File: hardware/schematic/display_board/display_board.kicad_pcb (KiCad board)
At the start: 2 copper layers, 52.5 x 49 mm, 7 parts, among them J1 Conn_01x04_Pin, SW1 SW_Push, SW2 SW_Push

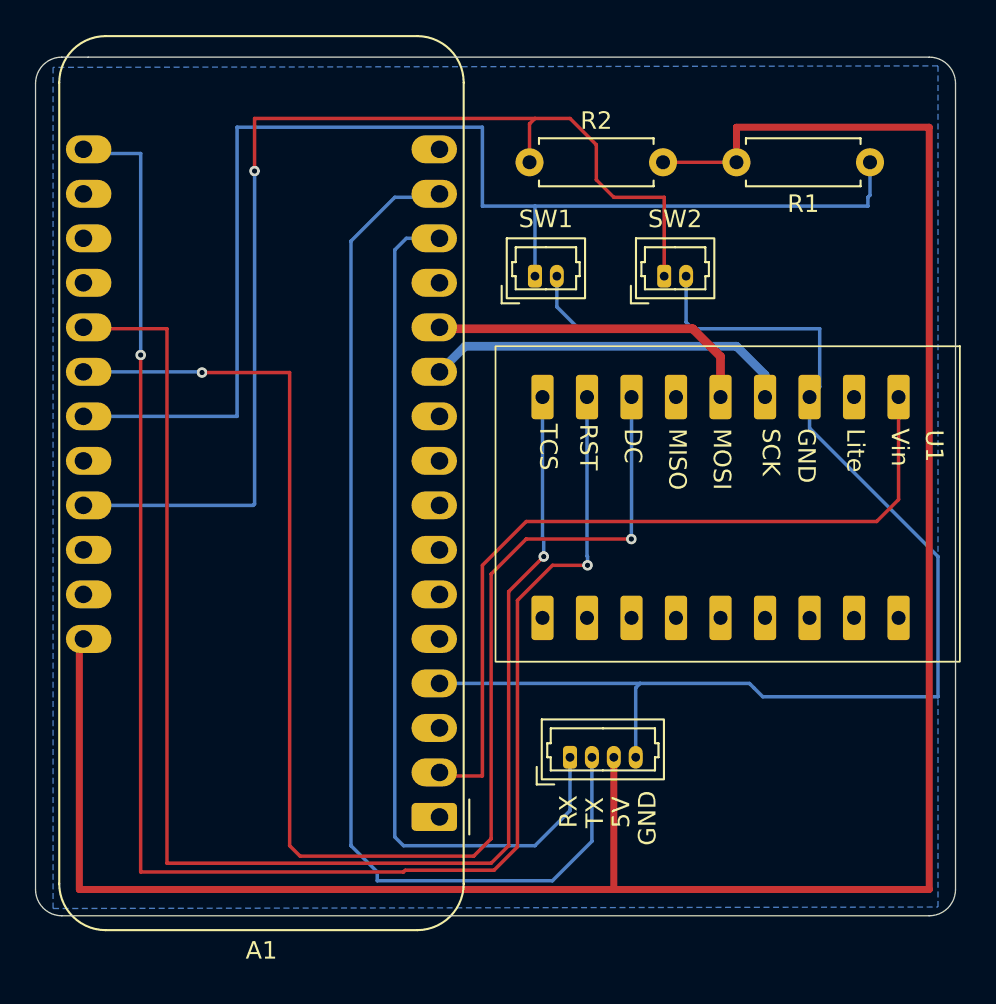
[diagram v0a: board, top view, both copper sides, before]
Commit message: First commit of PCB files for NAV and DISPLAY boards
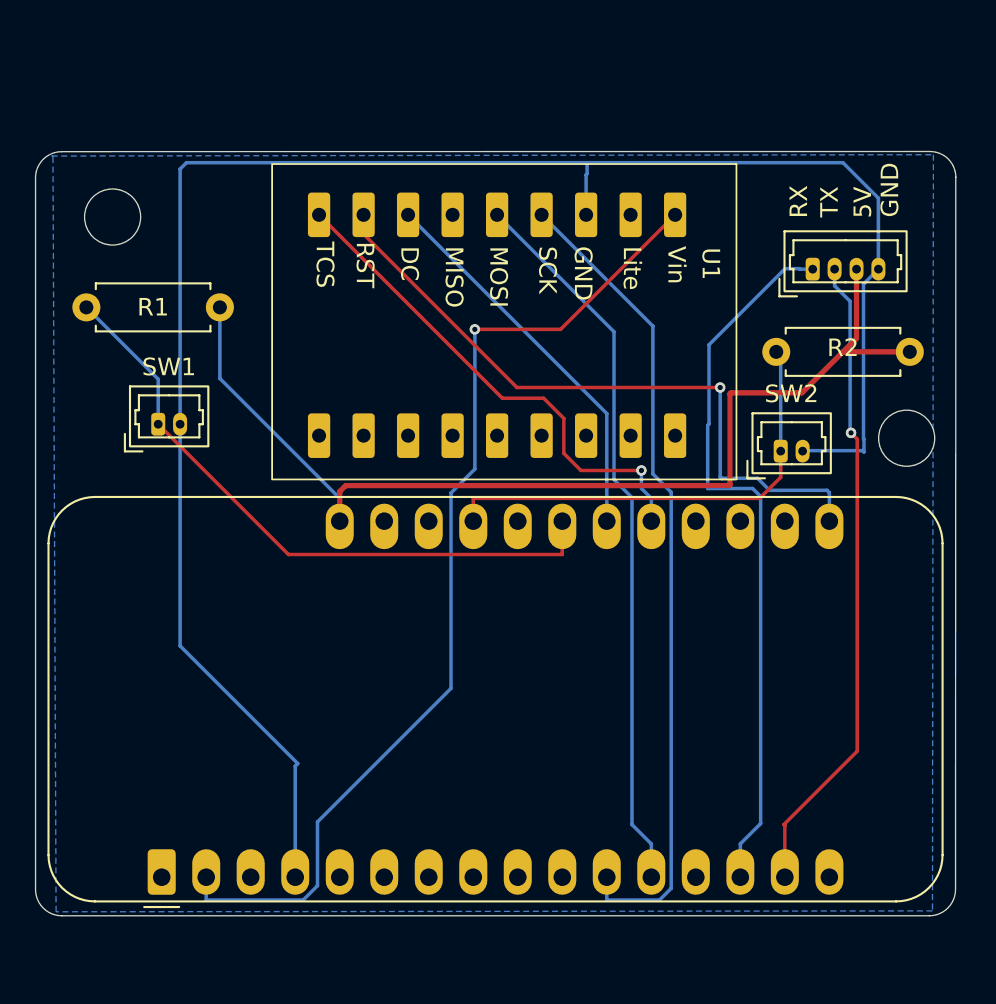
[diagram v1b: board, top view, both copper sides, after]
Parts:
- added REF**: MountingHole_3.2mm_M3_DIN965, MountingHole:MountingHole_3.2mm_M3_DIN965, F.Cu at (135.7, 88.7)
- added REF**: MountingHole_3.2mm_M3_DIN965, MountingHole:MountingHole_3.2mm_M3_DIN965, F.Cu at (90.4, 76.1)
- moved R1 45.5 mm to (88.9, 81.3), turned to 0 degrees
- moved J1 31.1 mm to (130.3, 79.1)
- moved SW1 23.1 mm to (93.0, 88.0)
- moved R2 17.8 mm to (128.3, 83.8)
- moved U1 16.5 mm to (122.5, 76.0)
- moved A1 16.2 mm to (93.2, 113.8), turned to 90 degrees
- moved SW2 12.0 mm to (128.5, 89.5)
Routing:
- net +5V: track 130.9 -> 60.9 mm
- net Net-(A1-A9/IO33): track 83.0 -> 22.2 mm, vias 2 -> 0
- net Net-(A1-SDA/IO23): track 95.0 -> 38.4 mm, vias 2 -> 1
- net /DC: track 81.7 -> 28.7 mm
- net Net-(A1-A12/IO13): track 65.3 -> 26.6 mm, vias 1 -> 0
- net Net-(A1-A10/IO27): track 72.5 -> 36.4 mm
- net GND: track 77.8 -> 105.5 mm
- net /MOSI: track 21.1 -> 46.8 mm
- net Net-(A1-TX/IO17): track 61.3 -> 37.0 mm, vias 0 -> 1
- net Net-(A1-MOSI/IO18): track 19.3 -> 41.4 mm
- net /3V3: track 45.9 -> 57.6 mm, vias 0 -> 1
- net Net-(A1-RX/IO16): track 50.9 -> 41.4 mm
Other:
- board size 52.5 x 49 mm -> 52.5 x 43.6 mm
